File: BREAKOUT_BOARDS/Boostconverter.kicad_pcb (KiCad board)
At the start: 4 copper layers, 37 parts, among them J1 POWERIN, J2 POWEROUT, Q1 TBD_N, Q2 TBD_N, Q3 TBD_N, Q4 TBD_N, U1 LM5175RHF

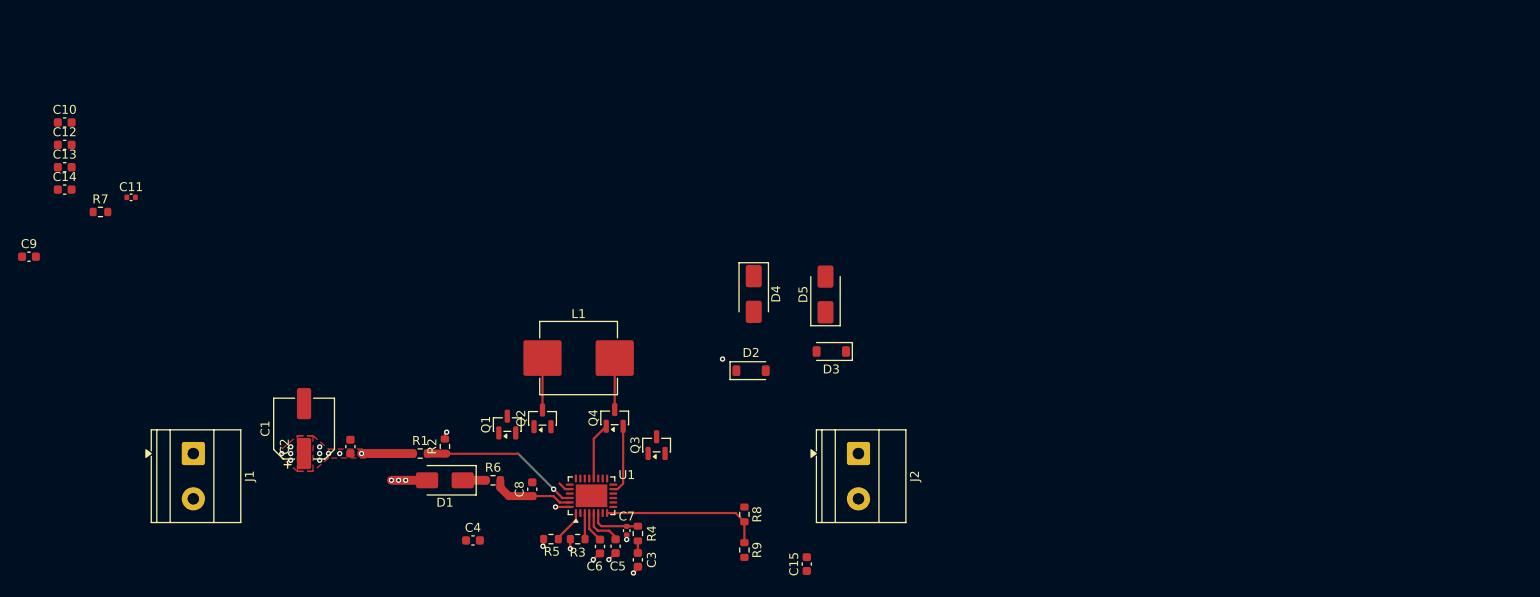
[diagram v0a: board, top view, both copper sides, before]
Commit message: Routing 1
Completed all footprint and part sourcing. Completed half of the routing.
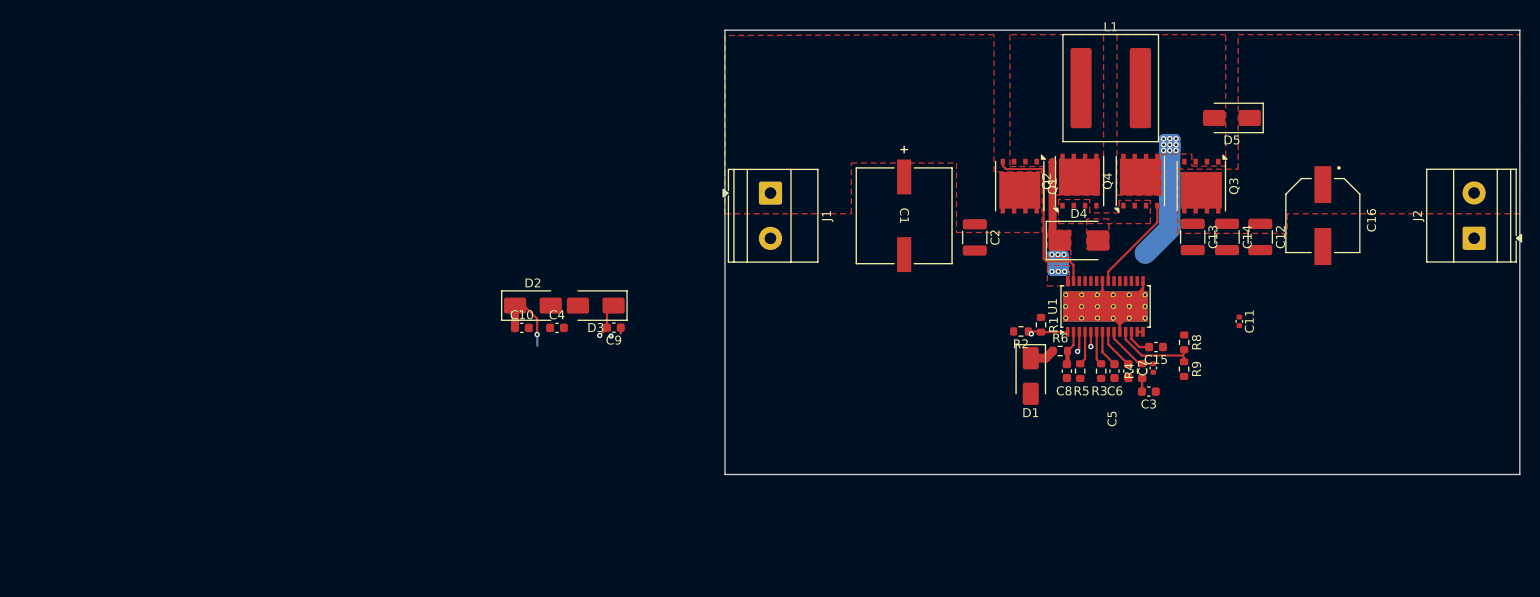
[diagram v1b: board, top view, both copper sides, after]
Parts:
- removed R7: 8m, Resistor_SMD:R_0603_1608Metric
- added C16: 82u, MyFootprintLibrary:CAP_35SVPF82M, F.Cu at (227.1, 52.3)
- C1: footprint Capacitor_SMD:CP_Elec_6.3x5.4 -> MyFootprintLibrary:PCAP_SVP_F12_PAN-M
- C12, C13, C14, C2: footprint Capacitor_SMD:C_0603_1608Metric -> Capacitor_SMD:C_1210_3225Metric
- C5: value 22n -> 68n
- C7: value 47p -> 33p
- D1, D5: value SS54 -> SS14
- D2, D3: value B5819W SL -> SS14; footprint Diode_SMD:D_SOD-123 -> Diode_SMD:D_SMA
- D4: value SS54 -> SK104B; footprint Diode_SMD:D_SMA -> Diode_SMD:D_SMB
- L1: value 3.3u -> 2.2u; footprint Inductor_SMD:L_Panasonic_PCC-M0850M -> Inductor_SMD:L_Coilcraft_XAL1010-XXX
- Q1, Q2, Q3, Q4: value TBD_N -> NCEP60T15G; footprint Package_TO_SOT_SMD:SOT-23 -> MyFootprintLibrary:AO_DFN-8-1EP_5.55x5.2mm_P1.27mm_EP4.12x4.6mm
- R4: value 21k -> 26.7k
- U1: value LM5175RHF -> LM5175PWP; footprint Package_DFN_QFN:VQFN-28-1EP_4x5mm_P0.5mm_EP2.55x3.55mm -> Package_SO:HTSSOP-28-1EP_4.4x9.7mm_P0.65mm_EP3.4x9.5mm_ThermalVias
- moved C12 134.5 mm to (220.1, 54.7), turned to -90 degrees
- moved C14 130.5 mm to (216.3, 54.7), turned to -90 degrees
- moved C13 126.8 mm to (212.5, 54.7), turned to -90 degrees
- moved C11 125.1 mm to (217.7, 64.2), turned to -90 degrees
- moved C2 73.9 mm to (188.1, 54.8), turned to -90 degrees
- moved J2 73.2 mm to (244.1, 54.8), turned to 90 degrees
- moved C1 71.4 mm to (180.1, 52.3), turned to -90 degrees
- moved R1 71.1 mm to (195.5, 64.5), turned to -90 degrees
- moved J1 71.0 mm to (165.1, 49.8)
- moved Q3 67.7 mm to (213.5, 49.0), turned to -90 degrees
- moved L1 66.9 mm to (203.3, 38.0)
- moved D1 66.8 mm to (194.3, 70.3), turned to -90 degrees
- moved C9 66.1 mm to (147.6, 64.9), turned to 180 degrees
- moved R2 65.9 mm to (193.2, 65.3), turned to 180 degrees
- moved Q2 65.9 mm to (199.8, 48.4)
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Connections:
- D5 pad 2: Net-(D5-A) -> /SW2
- J2 pad 1: +24V -> GNDREF
- J2 pad 2: GNDREF -> +24V
- L1 pad 2: Net-(D5-A) -> /SW2
- Q3 pad 2: Net-(D5-A) -> /SW2
- Q4 pad 3: Net-(D5-A) -> /SW2
- R6 pad 1: Net-(D1-K) -> Net-(U1-VIN)
- R6 pad 2: Net-(U1-VIN) -> Net-(D1-K)
- U1 pad 1: Net-(U1-MODE) -> Net-(U1-EN/UVLO)
- U1 pad 10: Net-(U1-ISNS(+)) -> GNDREF
- U1 pad 11: Net-(U1-ISNS(+)) -> Net-(U1-FB)
- U1 pad 12: GNDREF -> Net-(U1-VOSNS)
- U1 pad 13: Net-(D4-A) -> Net-(U1-ISNS(+))
- U1 pad 14: unconnected-(U1-PGOOD-Pad14) -> Net-(U1-ISNS(+))
- U1 pad 15: /SW2 -> GNDREF
- U1 pad 16: /HDRV2 -> Net-(D4-A)
- U1 pad 17: Net-(D3-K) -> unconnected-(U1-PGOOD-Pad17)
- U1 pad 18: /LDRV2 -> /SW2
- U1 pad 19: GNDREF -> /HDRV2
- U1 pad 2: AGND -> Net-(U1-VIN)
- U1 pad 20: /VCC -> Net-(D3-K)
- U1 pad 21: +24V -> /LDRV2
- U1 pad 22: Net-(Q2-G) -> GNDREF
- U1 pad 23: Net-(D2-K) -> /VCC
- U1 pad 24: /HDRV1 -> +24V
- U1 pad 25: Net-(D4-K) -> Net-(Q2-G)
- U1 pad 26: Net-(U1-EN/UVLO) -> Net-(D2-K)
- U1 pad 27: Net-(U1-VIN) -> /HDRV1
- U1 pad 28: +12V -> Net-(D4-K)
- U1 pad 3: Net-(U1-RT/SYNC) -> +12V
- U1 pad 4: Net-(U1-SLOPE) -> Net-(U1-MODE)
- U1 pad 5: Net-(U1-SS) -> AGND
- U1 pad 6: Net-(U1-COMP) -> Net-(U1-RT/SYNC)
- U1 pad 7: GNDREF -> Net-(U1-SLOPE)
- U1 pad 8: Net-(U1-FB) -> Net-(U1-SS)
- U1 pad 9: Net-(U1-VOSNS) -> Net-(U1-COMP)
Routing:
- net +12V: track 50.6 -> 2.28 mm, vias 14 -> 1
- net /SW2: track 0.00 -> 21.0 mm, vias 0 -> 10
- net /HDRV1: track 1.43 -> 20.6 mm
- net GNDREF: track 0.86 -> 17.9 mm, vias 1 -> 0
- net Net-(U1-EN/UVLO): track 18.2 -> 4.46 mm, vias 2 -> 1
- net Net-(D4-K): track 5.83 -> 17.8 mm, vias 0 -> 6
- net Net-(U1-FB): track 18.2 -> 9.67 mm
- net Net-(D4-A): track 7.80 -> 0.00 mm
- net Net-(D2-K): track 0.00 -> 7.68 mm, vias 0 -> 1
- net Net-(D5-A): track 5.86 -> 0.00 mm
- net Net-(U1-VIN): track 9.30 -> 3.98 mm
- net /LDRV2: track 6.44 -> 10.7 mm
- net Net-(D3-K): track 0.00 -> 4.03 mm, vias 0 -> 1
- net AGND: track 5.53 -> 1.65 mm, vias 6 -> 1
- net Net-(U1-VOSNS): track 0.00 -> 3.15 mm
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- added copper zone on F.Cu, net +24V
- added copper zone on F.Cu, net /SW2
- added copper zone on F.Cu, net Net-(D4-A)
- added copper zone on F.Cu, net Net-(D4-K)
- removed copper zone on In2.Cu, net +12V
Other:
- board outline added: 89.2 x 49.8 mm

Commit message: Add files via upload
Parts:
- added R7: 5m, Resistor_SMD:R_1206_3216Metric, F.Cu at (206.0, 54.1)
- moved C4 70.3 mm to (211.5, 63.3)
- moved C9 59.7 mm to (206.9, 58.4)
- moved C10 58.6 mm to (195.8, 65.4), turned to 90 degrees
- moved D2 54.6 mm to (193.1, 63.3), turned to 90 degrees
- moved D3 44.0 mm to (189.5, 63.3), turned to 90 degrees
- moved C11 9.95 mm to (208.0, 62.3), turned to 0 degrees
- moved C15 4.19 mm to (209.7, 71.0)
- moved C3 4.19 mm to (208.9, 76.0)
- moved C5 4.19 mm to (206.6, 73.7)
- moved C6 4.19 mm to (205.1, 73.7)
- moved C7 4.19 mm to (209.4, 73.4)
- moved C8 4.19 mm to (199.7, 73.7)
- moved R1 4.19 mm to (196.8, 68.5)
- moved R2 4.19 mm to (194.6, 69.3)
- moved R3 4.19 mm to (203.6, 73.7)
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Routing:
- net +12V: track 2.28 -> 31.1 mm, vias 1 -> 4
- net Net-(Q2-G): track 0.00 -> 22.6 mm
- net /HDRV2: track 0.00 -> 21.0 mm, vias 0 -> 2
- net Net-(D3-K): track 4.03 -> 23.0 mm, vias 1 -> 2
- net Net-(D4-K): track 17.8 -> 0.00 mm, vias 6 -> 24
- net /VCC: track 0.03 -> 16.1 mm, vias 0 -> 2
- net +24V: track 0.00 -> 13.9 mm, vias 0 -> 2
- net Net-(D4-A): track 0.00 -> 13.0 mm, vias 0 -> 2
- net GNDREF: track 17.9 -> 27.9 mm, vias 0 -> 2
- net /HDRV1: track 20.6 -> 25.4 mm
- net /LDRV2: track 10.7 -> 15.3 mm
- net Net-(D2-K): track 7.68 -> 10.5 mm, vias 1 -> 2
- net /SW2: track 21.0 -> 20.0 mm, vias 10 -> 0
- net Net-(U1-EN/UVLO): vias 1 -> 0
- added copper zone on In2.Cu, net Net-(D4-K)
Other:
- board size 89.2 x 49.8 mm -> 89.2 x 48.2 mm

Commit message: edit boost converter, added gnd planes, polish later
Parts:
- moved C4 11.0 mm to (201.3, 59.2)
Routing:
- net +24V: track 13.9 -> 39.6 mm
- net Net-(D2-K): track 10.5 -> 13.6 mm
- net Net-(D4-A): track 13.0 -> 15.6 mm
- net Net-(U1-SLOPE): track 4.18 -> 6.21 mm
- net Net-(D4-K): track 0.00 -> 2.02 mm
- net AGND: track 1.65 -> 3.60 mm
- net /VCC: track 16.1 -> 17.7 mm
- net (no net): track 0.00 -> 1.00 mm
- added copper zone on F.Cu, net AGND
- added copper zone on F.Cu, net GNDREF
- added copper zone on In1.Cu, net GNDREF
